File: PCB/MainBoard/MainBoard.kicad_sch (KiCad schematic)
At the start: 17 parts, among them J1 PiPowerSwitch, J2 Pi_Zero, J3 I2C0, J4 JMD0.96C, J5 WS2812, J6 Extra_Keys, J8 JoyStick_Or_I2C1, SW1 SPI_SW, SW2 RotaryEncoder_Switch, U1 Pico

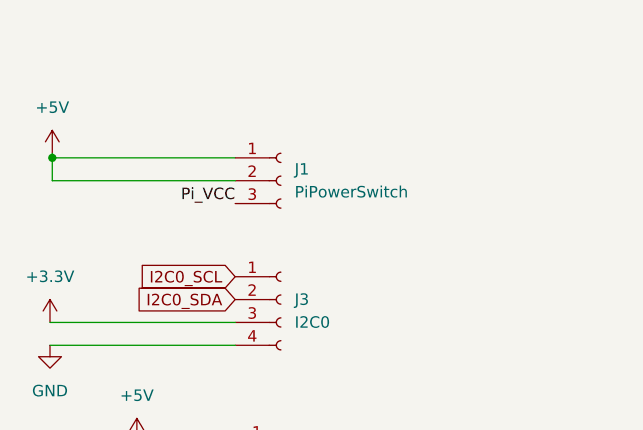
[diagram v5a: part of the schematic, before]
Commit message: Use switch instead of jumper
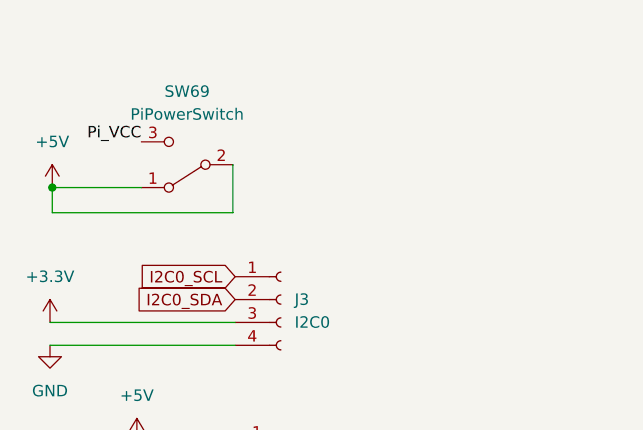
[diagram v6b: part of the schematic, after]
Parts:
- removed J1: PiPowerSwitch, Connector_PinHeader_2.54mm:PinHeader_1x03_P2.54mm_Vertical, symbol Connector:Conn_01x03_Female
- added SW69: PiPowerSwitch, Connector_PinHeader_2.54mm:PinHeader_1x03_P2.54mm_Vertical, symbol Switch:SW_SPDT
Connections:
- net +5V: now also SW69.1 (A), SW69.2 (B)
- net Pi_VCC: now also SW69.3 (C)
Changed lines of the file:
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@@
   (junction (at 235.712 50.8) (diameter 0) (color 0 0 0 0)
   )
-  (junction (at 28.956 36.576) (diameter 0) (color 0 0 0 0)
-  )
   (junction (at 244.094 81.28) (diameter 0) (color 0 0 0 0)
   )
   (junction (at 151.638 79.756) (diameter 0) (color 0 0 0 0)
   )
+  (junction (at 28.956 39.878) (diameter 0) (color 0 0 0 0)
+  )
   (junction (at 119.634 179.324) (diameter 0) (color 0 0 0 0)
   )
@@
     (stroke (width 0) (type default))
   )
-  (wire (pts (xy 49.276 36.576) (xy 28.956 36.576))
-    (stroke (width 0) (type default))
-  )
   (wire (pts (xy 144.78 31.496) (xy 144.78 28.956))
     (stroke (width 0) (type default))
@@
     (stroke (width 0) (type default))
   )
+  (wire (pts (xy 28.956 42.672) (xy 28.956 39.878))
+    (stroke (width 0) (type default))
+  )
   (wire (pts (xy 119.634 142.494) (xy 125.984 142.494))
     (stroke (width 0) (type default))
@@
     (stroke (width 0) (type default))
   )
-  (wire (pts (xy 28.956 36.068) (xy 28.956 36.576))
+  (wire (pts (xy 28.956 39.878) (xy 38.862 39.878))
     (stroke (width 0) (type default))
   )
@@
     (stroke (width 0) (type default))
   )
-  (wire (pts (xy 28.956 39.116) (xy 28.956 36.576))
-    (stroke (width 0) (type default))
-  )
   (wire (pts (xy 116.332 39.116) (xy 116.332 59.436))
     (stroke (width 0) (type default))
@@
     (stroke (width 0) (type default))
   )
-  (wire (pts (xy 49.276 39.116) (xy 28.956 39.116))
-    (stroke (width 0) (type default))
-  )
   (wire (pts (xy 129.286 39.116) (xy 116.332 39.116))
     (stroke (width 0) (type default))
   )
   (wire (pts (xy 119.634 150.114) (xy 125.73 150.114))
+    (stroke (width 0) (type default))
+  )
+  (wire (pts (xy 49.022 42.672) (xy 28.956 42.672))
+    (stroke (width 0) (type default))
+  )
+  (wire (pts (xy 49.022 37.338) (xy 49.022 42.672))
     (stroke (width 0) (type default))
   )
@@
     (effects (font (size 1.27 1.27)) (justify left bottom))
   )
-  (label "Pi_VCC" (at 49.276 41.656 180) (fields_autoplaced)
+  (label "Pi_VCC" (at 38.862 34.798 180) (fields_autoplaced)
     (effects (font (size 1.27 1.27)) (justify right bottom))
   )
@@
         (path "/bae0810c-de5c-4877-9e50-ea2ffd613142"
           (reference "J2") (unit 1)
+        )
+      )
+    )
+  )
+  (symbol (lib_id "Switch:SW_SPDT") (at 43.942 37.338 180) (unit 1)
+    (in_bom yes) (on_board yes) (dnp no) (fields_autoplaced)
+    (property "Reference" "SW69" (at 43.942 29.21 0)
+      (effects (font (size 1.27 1.27)))
+    )
+    (property "Value" "PiPowerSwitch" (at 43.942 31.75 0)
+      (effects (font (size 1.27 1.27)))
+    )
+    (property "Footprint" "Connector_PinHeader_2.54mm:PinHeader_1x03_P2.54mm_Vertical" (at 43.942 37.338 0)
+      (effects (font (size 1.27 1.27)) hide)
+    )
+    (property "Datasheet" "~" (at 43.942 37.338 0)
+      (effects (font (size 1.27 1.27)) hide)
+    )
+    (pin "1")
+    (pin "2")
+    (pin "3")
+    (instances
+      (project "MainBoard"
+        (path "/bae0810c-de5c-4877-9e50-ea2ffd613142"
+          (reference "SW69") (unit 1)
         )
       )
@@
     )
   )
-  (symbol (lib_id "Connector:Conn_01x03_Female") (at 54.356 39.116 0) (unit 1)
-    (in_bom yes) (on_board yes) (dnp no) (fields_autoplaced)
-    (property "Reference" "J1" (at 55.88 37.846 0)
-      (effects (font (size 1.27 1.27)) (justify left))
-    )
-    (property "Value" "PiPowerSwitch" (at 55.88 40.386 0)
-      (effects (font (size 1.27 1.27)) (justify left))
-    )
-    (property "Footprint" "Connector_PinHeader_2.54mm:PinHeader_1x03_P2.54mm_Vertical" (at 54.356 39.116 0)
-      (effects (font (size 1.27 1.27)) hide)
-    )
-    (property "Datasheet" "~" (at 54.356 39.116 0)
-      (effects (font (size 1.27 1.27)) hide)
-    )
-    (pin "1")
-    (pin "2")
-    (pin "3")
-    (instances
-      (project "MainBoard"
-        (path "/bae0810c-de5c-4877-9e50-ea2ffd613142"
-          (reference "J1") (unit 1)
-        )
-      )
-    )
-  )
   (symbol (lib_id "power:+3V3") (at 96.774 152.654 0) (unit 1)
     (in_bom yes) (on_board yes) (dnp no) (fields_autoplaced)
@@
     )
   )
-  (symbol (lib_id "power:+5V") (at 28.956 36.068 0) (unit 1)
-    (in_bom yes) (on_board yes) (dnp no) (fields_autoplaced)
-    (property "Reference" "#PWR01" (at 28.956 39.878 0)
-      (effects (font (size 1.27 1.27)) hide)
-    )
-    (property "Value" "+5V" (at 28.956 30.988 0)
-      (effects (font (size 1.27 1.27)))
-    )
-    (property "Footprint" "" (at 28.956 36.068 0)
-      (effects (font (size 1.27 1.27)) hide)
-    )
-    (property "Datasheet" "" (at 28.956 36.068 0)
-      (effects (font (size 1.27 1.27)) hide)
-    )
+  (symbol (lib_id "power:+5V") (at 28.956 39.878 0) (unit 1)
+    (in_bom yes) (on_board yes) (dnp no) (fields_autoplaced)
+    (property "Reference" "#PWR01" (at 28.956 43.688 0)
+      (effects (font (size 1.27 1.27)) hide)
+    )
+    (property "Value" "+5V" (at 28.956 34.798 0)
+      (effects (font (size 1.27 1.27)))
+    )
+    (property "Footprint" "" (at 28.956 39.878 0)
+      (effects (font (size 1.27 1.27)) hide)
+    )
+    (property "Datasheet" "" (at 28.956 39.878 0)
+      (effects (font (size 1.27 1.27)) hide)
+    )

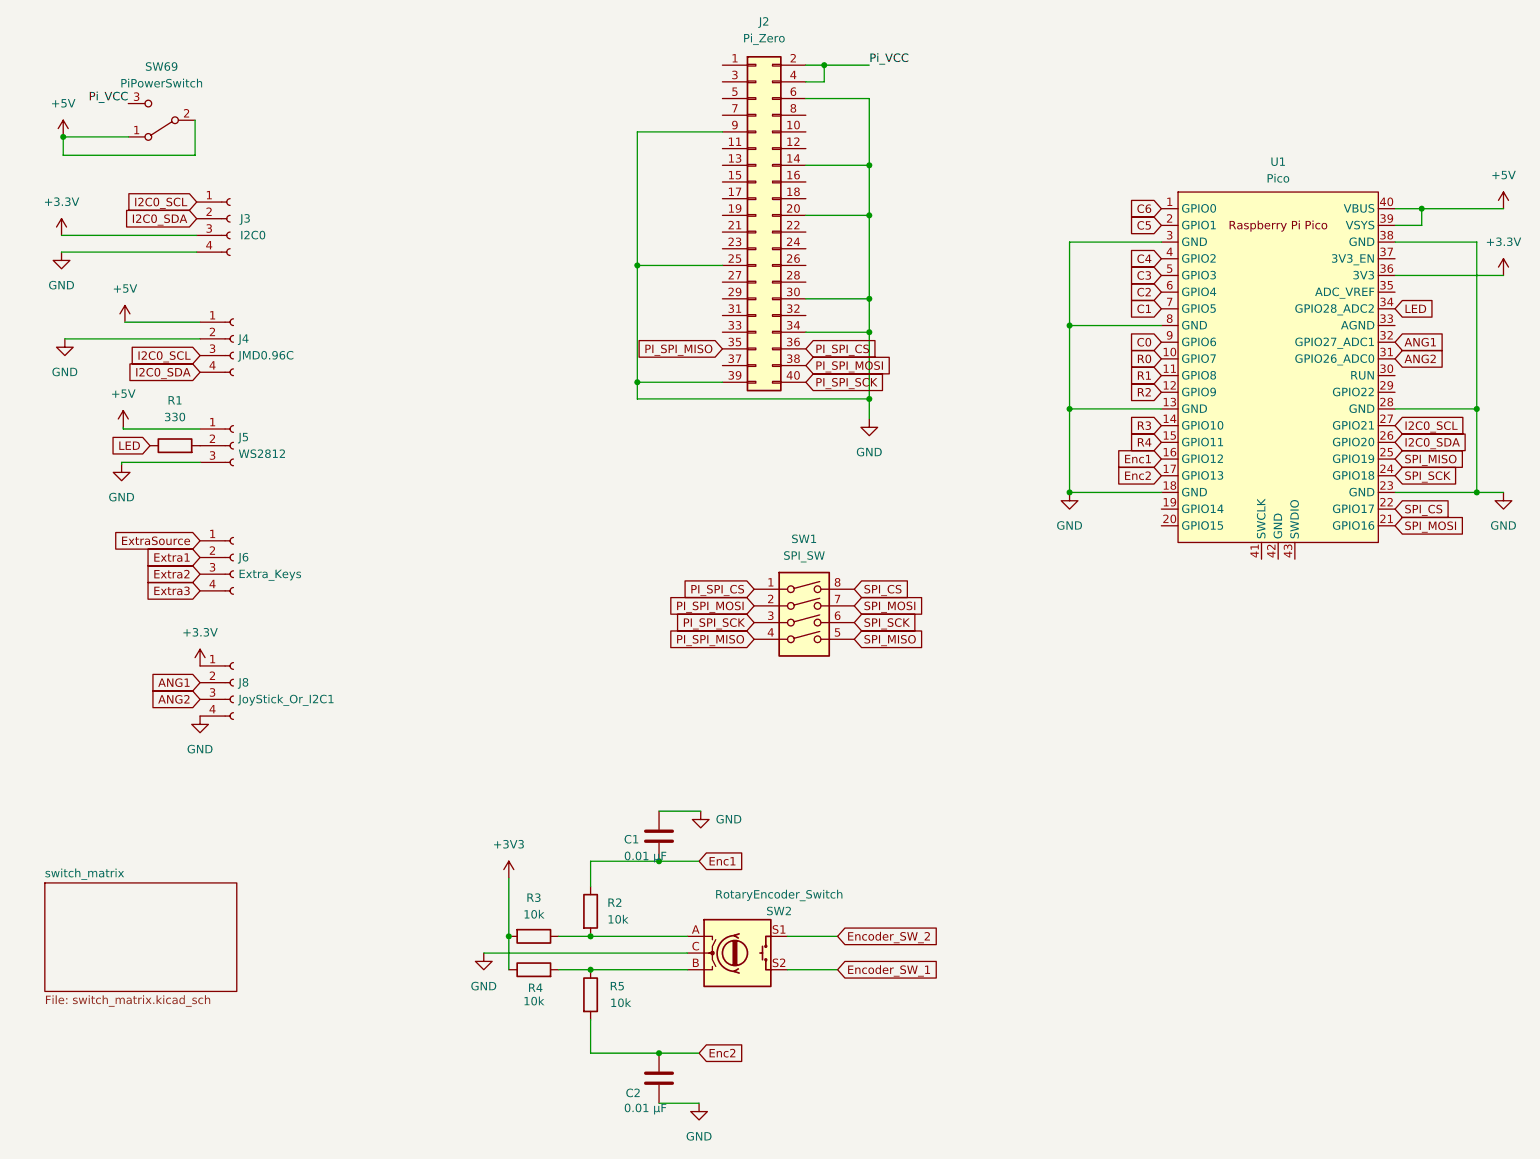
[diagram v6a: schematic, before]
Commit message: Updated the bottom connector, and replotted the files
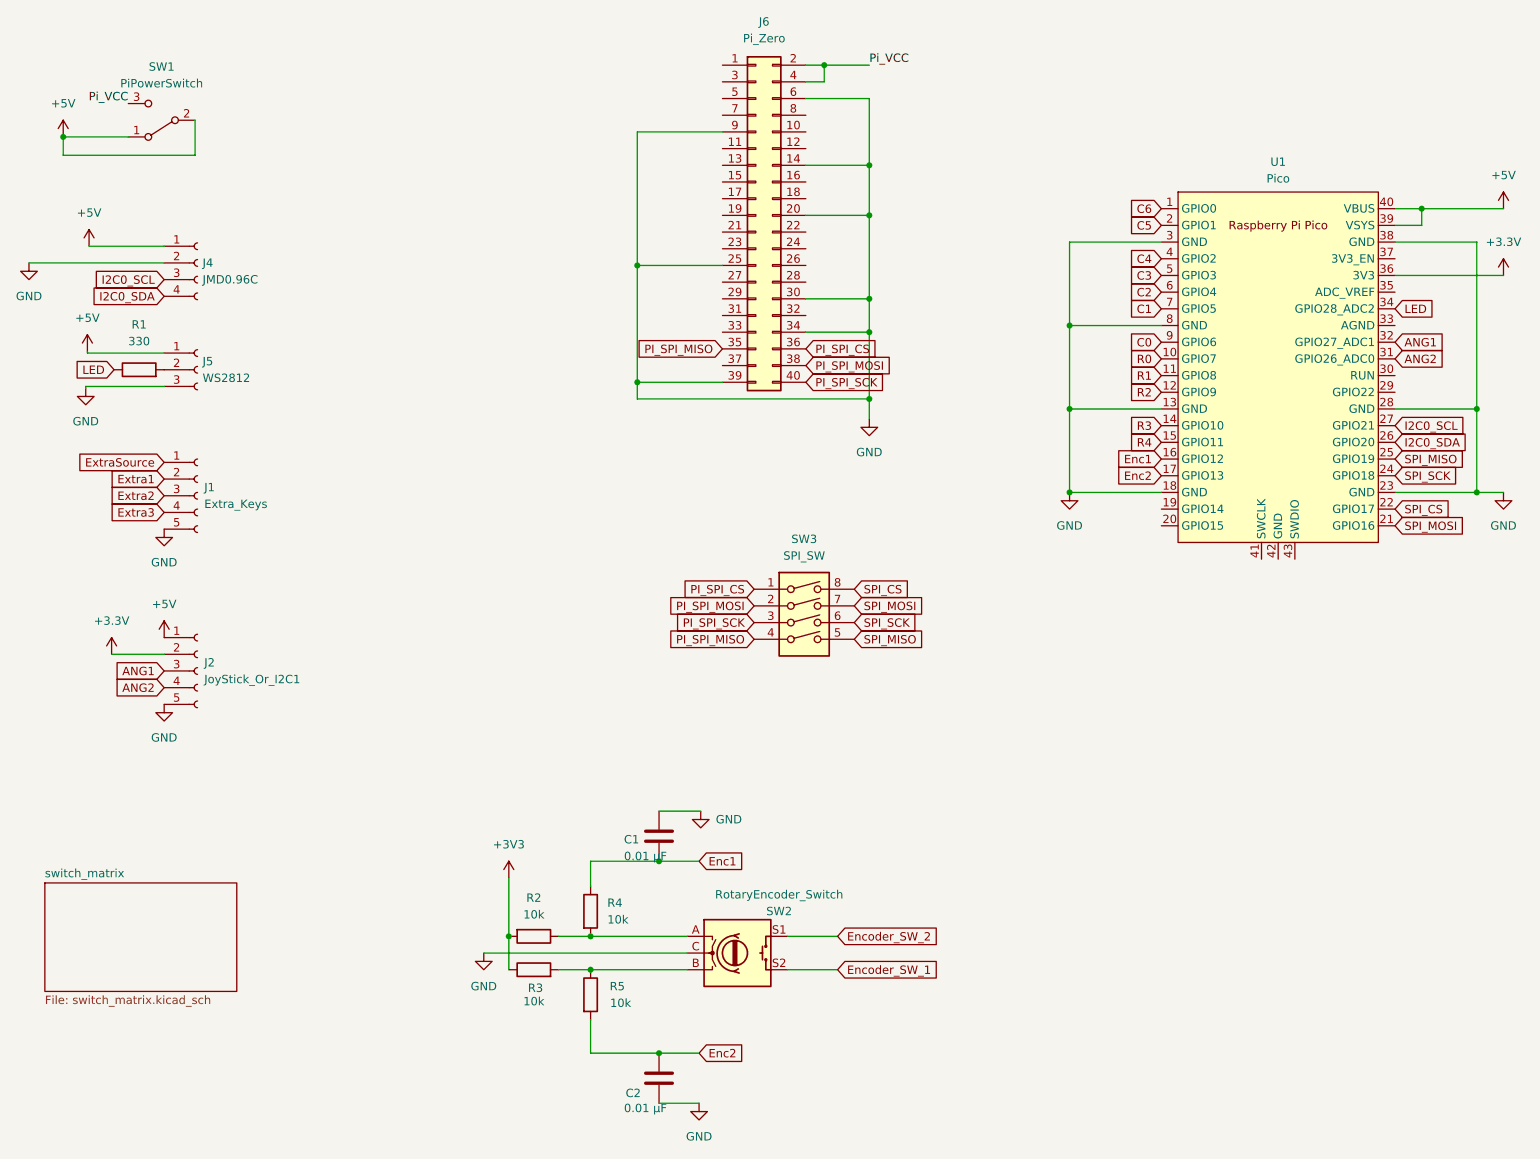
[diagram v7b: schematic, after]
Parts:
- removed J3: I2C0, Connector_PinHeader_2.54mm:PinHeader_1x04_P2.54mm_Horizontal, symbol Connector:Conn_01x04_Female
- removed J6: Extra_Keys, Connector_JST:JST_PH_S4B-PH-K_1x04_P2.00mm_Horizontal, symbol Connector:Conn_01x04_Female
- removed J8: JoyStick_Or_I2C1, Connector_JST:JST_PH_S4B-PH-K_1x04_P2.00mm_Horizontal, symbol Connector:Conn_01x04_Female
- added J1: Extra_Keys, Connector_PinSocket_2.54mm:PinSocket_1x05_P2.54mm_Horizontal, symbol Connector:Conn_01x05_Socket
- added J2: JoyStick_Or_I2C1, Connector_PinSocket_2.54mm:PinSocket_1x05_P2.54mm_Horizontal, symbol Connector:Conn_01x05_Socket
- renumbered J2 to J6, R3 to R2, R4 to R3, R2 to R4, SW69 to SW1, SW1 to SW3
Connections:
- net +3V3: now also J2.2 (Pin_2)
- net +5V: now also J2.1 (Pin_1)
- net ANG1: now also J2.3 (Pin_3)
- net ANG2: now also J2.4 (Pin_4)
- net Extra1: now also J1.2 (Pin_2)
- net Extra2: now also J1.3 (Pin_3)
- net Extra3: now also J1.4 (Pin_4)
- net ExtraSource: now also J1.1 (Pin_1)
- net GND: now also J1.5 (Pin_5), J2.5 (Pin_5)
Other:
- moved on the sheet: J4, J5, R1

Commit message: Added SMT pads to the diodes
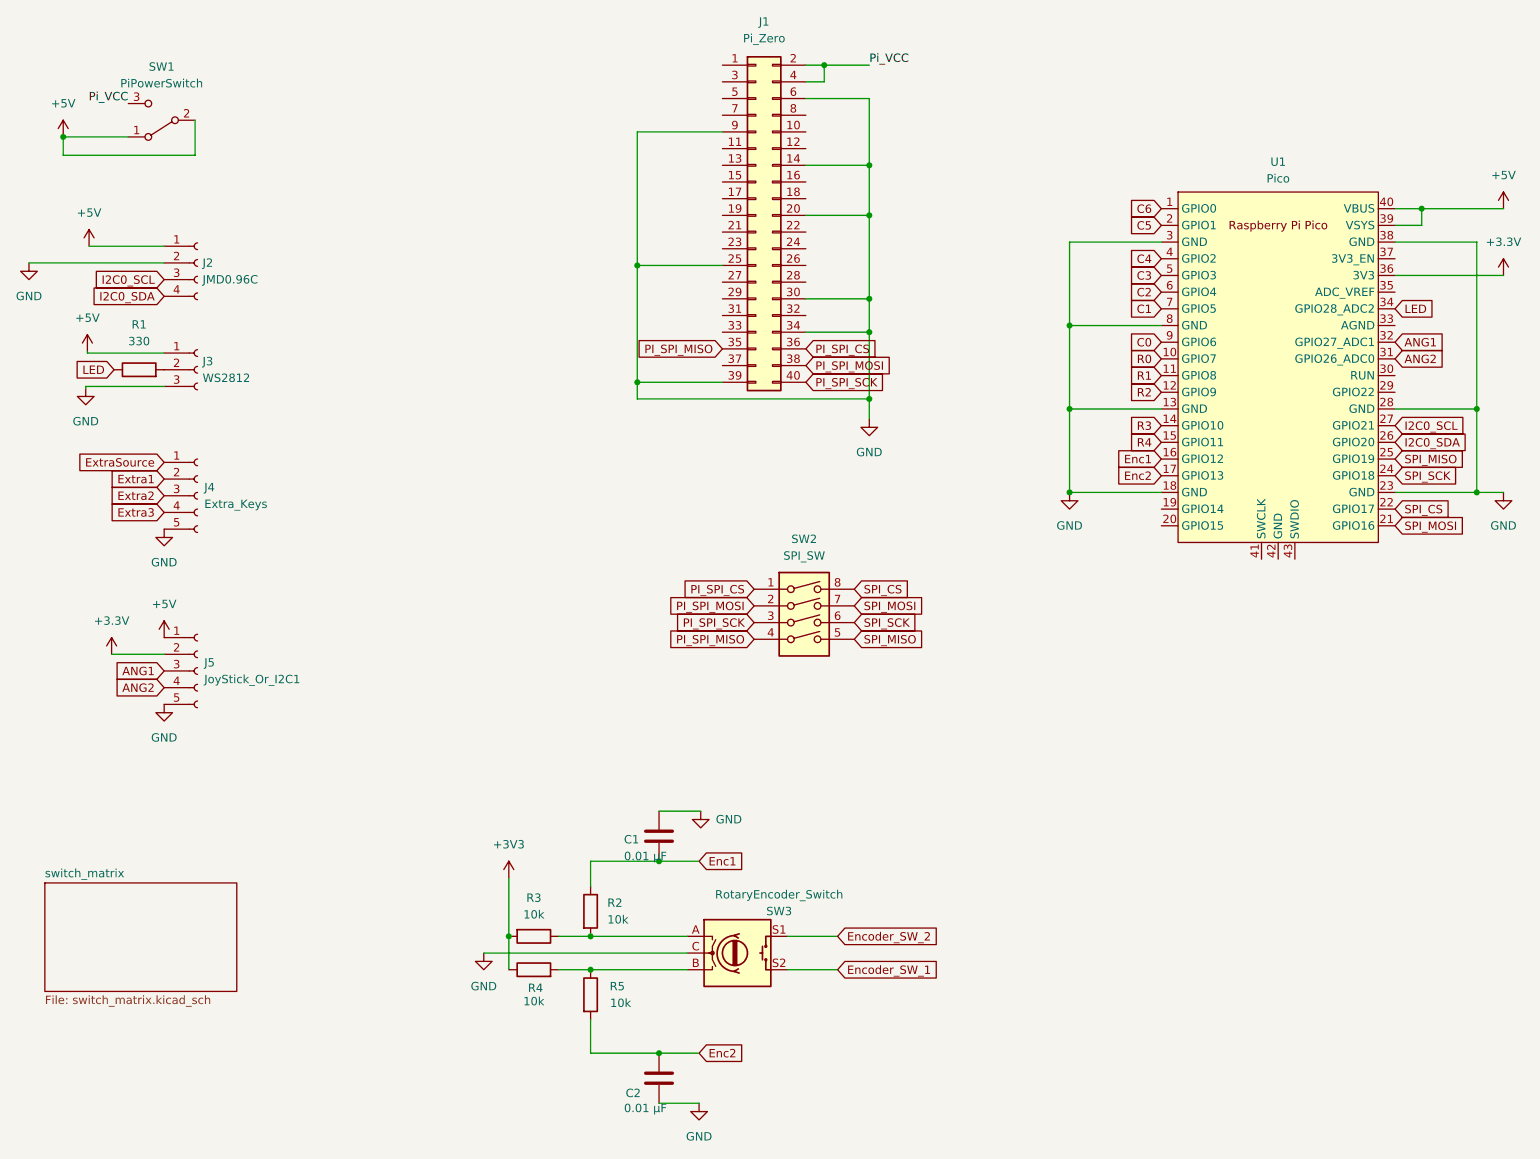
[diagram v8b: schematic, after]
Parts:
- renumbered J6 to J1, J4 to J2, J5 to J3, J1 to J4, J2 to J5, R4 to R2, R2 to R3, R3 to R4, SW3 to SW2, SW2 to SW3
